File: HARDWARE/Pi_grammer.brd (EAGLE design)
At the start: 85.1 x 78.7 mm, 28 parts, among them J2 TARGET_copy, J3 TESTBED, J4 CABLE, U1 AT42QT1010SOT23

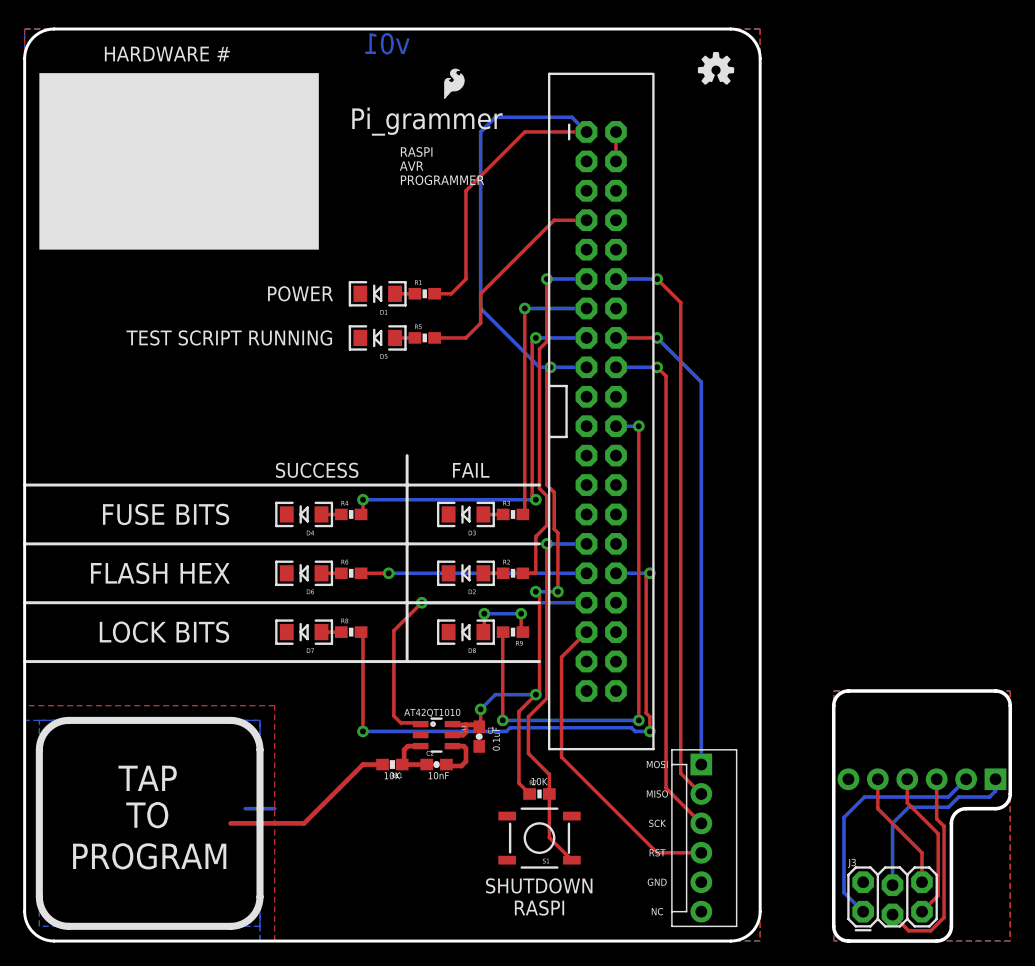
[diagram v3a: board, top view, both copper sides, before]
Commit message: changes "script running" led silk to "STAT"
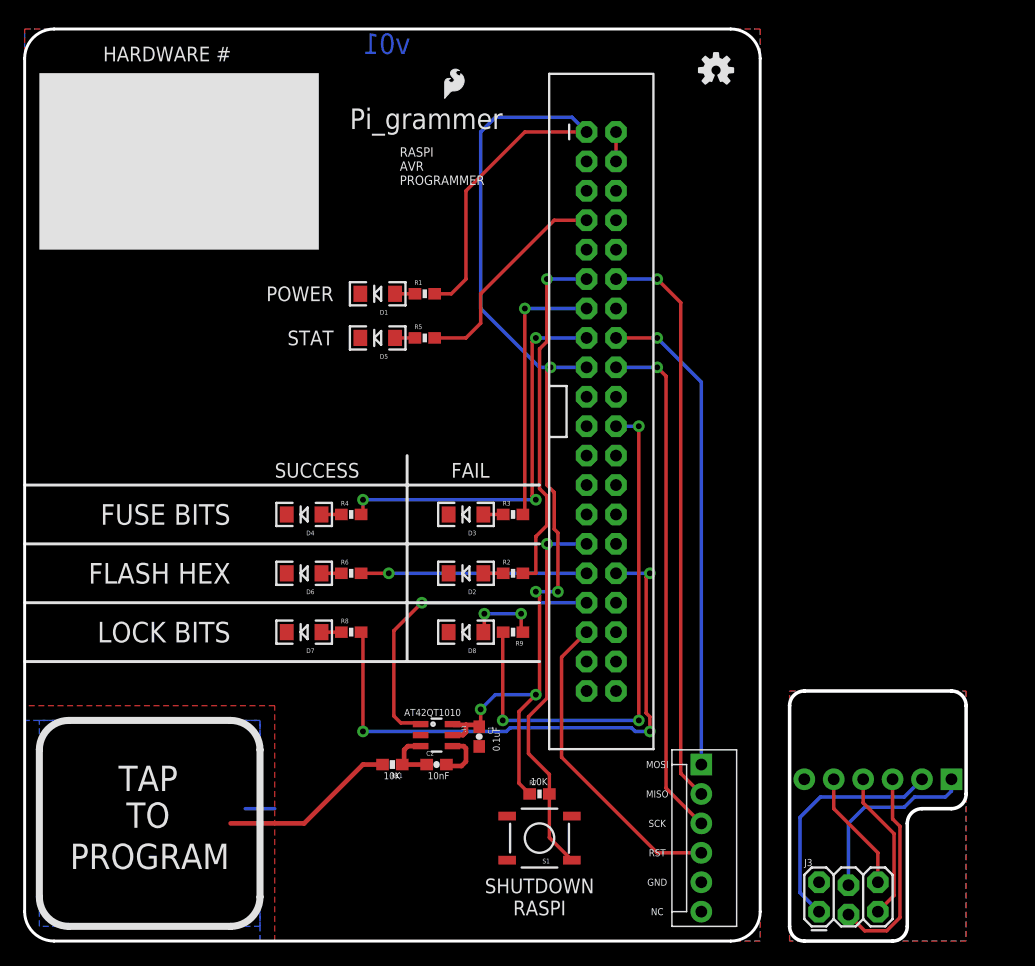
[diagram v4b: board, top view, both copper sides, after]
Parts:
- moved J3 3.81 mm to (68.6, 2.54)
- moved J4 3.81 mm to (80.0, 14.0)
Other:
- board size 85.1 x 78.7 mm -> 81.3 x 78.7 mm
- board text added: "STAT"
- board text removed: "TEST SCRIPT RUNNING"
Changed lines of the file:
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@@
 <layer number="47" name="Measures" color="7" fill="1" visible="no" active="yes"/>
 <layer number="48" name="Document" color="7" fill="1" visible="no" active="yes"/>
-<layer number="49" name="Reference" color="7" fill="1" visible="yes" active="yes"/>
+<layer number="49" name="Reference" color="7" fill="1" visible="no" active="yes"/>
 <layer number="50" name="dxf" color="7" fill="1" visible="no" active="yes"/>
 <layer number="51" name="tDocu" color="6" fill="1" visible="yes" active="yes"/>
@@
 <text x="28.067" y="70.104" size="1.778" layer="21" font="vector" ratio="15">Pi_grammer</text>
 <text x="6.7724375" y="75.946675" size="1.27" layer="21" font="vector" ratio="15">HARDWARE #</text>
-<text x="26.67" y="52.07" size="1.27" layer="21" font="vector" ratio="15" align="center-right">TEST SCRIPT RUNNING</text>
+<text x="26.67" y="52.07" size="1.27" layer="21" font="vector" ratio="15" align="center-right">STAT</text>
 <text x="17.78" y="36.83" size="1.778" layer="21" font="vector" ratio="15" align="center-right">FUSE BITS</text>
 <text x="26.67" y="55.88" size="1.27" layer="21" font="vector" ratio="15" align="center-right">POWER</text>
@@
 <text x="54.61" y="5.08" size="0.6096" layer="21" font="vector" ratio="15" align="center">GND</text>
 <text x="54.61" y="2.54" size="0.6096" layer="21" font="vector" ratio="15" align="center">NC</text>
-<wire x1="80.01" y1="1.27" x2="78.74" y2="0" width="0.3048" layer="20" curve="-90"/>
-<wire x1="78.74" y1="0" x2="71.12" y2="0" width="0.3048" layer="20"/>
-<wire x1="71.12" y1="0" x2="69.85" y2="1.27" width="0.3048" layer="20" curve="-90"/>
-<wire x1="69.85" y1="1.27" x2="69.85" y2="20.32" width="0.3048" layer="20"/>
-<wire x1="69.85" y1="20.32" x2="71.12" y2="21.59" width="0.3048" layer="20" curve="-90"/>
-<wire x1="71.12" y1="21.59" x2="83.82" y2="21.59" width="0.3048" layer="20"/>
-<wire x1="83.82" y1="21.59" x2="85.09" y2="20.32" width="0.3048" layer="20" curve="-90"/>
-<wire x1="85.09" y1="20.32" x2="85.09" y2="12.7" width="0.3048" layer="20"/>
-<wire x1="85.09" y1="12.7" x2="83.82" y2="11.43" width="0.3048" layer="20" curve="-90"/>
-<wire x1="83.82" y1="11.43" x2="81.28" y2="11.43" width="0.3048" layer="20"/>
-<wire x1="81.28" y1="11.43" x2="80.01" y2="10.16" width="0.3048" layer="20" curve="90"/>
-<wire x1="80.01" y1="10.16" x2="80.01" y2="1.27" width="0.3048" layer="20"/>
+<wire x1="76.2" y1="1.27" x2="74.93" y2="0" width="0.3048" layer="20" curve="-90"/>
+<wire x1="74.93" y1="0" x2="67.31" y2="0" width="0.3048" layer="20"/>
+<wire x1="67.31" y1="0" x2="66.04" y2="1.27" width="0.3048" layer="20" curve="-90"/>
+<wire x1="66.04" y1="1.27" x2="66.04" y2="20.32" width="0.3048" layer="20"/>
+<wire x1="66.04" y1="20.32" x2="67.31" y2="21.59" width="0.3048" layer="20" curve="-90"/>
+<wire x1="67.31" y1="21.59" x2="80.01" y2="21.59" width="0.3048" layer="20"/>
+<wire x1="80.01" y1="21.59" x2="81.28" y2="20.32" width="0.3048" layer="20" curve="-90"/>
+<wire x1="81.28" y1="20.32" x2="81.28" y2="12.7" width="0.3048" layer="20"/>
+<wire x1="81.28" y1="12.7" x2="80.01" y2="11.43" width="0.3048" layer="20" curve="-90"/>
+<wire x1="80.01" y1="11.43" x2="77.47" y2="11.43" width="0.3048" layer="20"/>
+<wire x1="77.47" y1="11.43" x2="76.2" y2="10.16" width="0.3048" layer="20" curve="90"/>
+<wire x1="76.2" y1="10.16" x2="76.2" y2="1.27" width="0.3048" layer="20"/>
 </plain>
 <attributes>
@@
 </element>
 <element name="J2" library="SparkFun-Connectors" package="MOLEX-1X6" value="TARGET_copy" x="58.42" y="15.24" rot="R270"/>
-<element name="J3" library="SparkFun-Connectors" package="2X3_LOCK" value="TESTBED" x="72.39" y="2.54"/>
-<element name="J4" library="SparkFun-Connectors" package="MOLEX-1X6-RA" value="CABLE" x="83.82" y="13.97" rot="MR0"/>
+<element name="J3" library="SparkFun-Connectors" package="2X3_LOCK" value="TESTBED" x="68.58" y="2.54"/>
+<element name="J4" library="SparkFun-Connectors" package="MOLEX-1X6-RA" value="CABLE" x="80.01" y="13.97" rot="MR0"/>
 </elements>
 <signals>
@@
 <contactref element="J4" pad="1"/>
 <contactref element="J3" pad="4"/>
-<wire x1="83.82" y1="13.97" x2="83.82" y2="12.954" width="0.3048" layer="16"/>
-<wire x1="83.82" y1="12.954" x2="83.312" y2="12.446" width="0.3048" layer="16"/>
-<wire x1="83.312" y1="12.446" x2="80.645" y2="12.446" width="0.3048" layer="16"/>
-<wire x1="80.645" y1="12.446" x2="79.756" y2="11.557" width="0.3048" layer="16"/>
-<wire x1="79.756" y1="11.557" x2="76.327" y2="11.557" width="0.3048" layer="16"/>
-<wire x1="76.327" y1="11.557" x2="74.93" y2="10.16" width="0.3048" layer="16"/>
-<wire x1="74.93" y1="10.16" x2="74.93" y2="4.826" width="0.3048" layer="16"/>
+<wire x1="80.01" y1="13.97" x2="80.01" y2="12.954" width="0.3048" layer="16"/>
+<wire x1="80.01" y1="12.954" x2="79.502" y2="12.446" width="0.3048" layer="16"/>
+<wire x1="79.502" y1="12.446" x2="76.835" y2="12.446" width="0.3048" layer="16"/>
+<wire x1="76.835" y1="12.446" x2="75.946" y2="11.557" width="0.3048" layer="16"/>
+<wire x1="75.946" y1="11.557" x2="72.517" y2="11.557" width="0.3048" layer="16"/>
+<wire x1="72.517" y1="11.557" x2="71.12" y2="10.16" width="0.3048" layer="16"/>
+<wire x1="71.12" y1="10.16" x2="71.12" y2="4.826" width="0.3048" layer="16"/>
 </signal>
 <signal name="MISO_C">
 <contactref element="J4" pad="2"/>
 <contactref element="J3" pad="1"/>
-<wire x1="81.28" y1="13.97" x2="79.756" y2="12.446" width="0.3048" layer="16"/>
-<wire x1="79.756" y1="12.446" x2="72.517" y2="12.446" width="0.3048" layer="16"/>
-<wire x1="72.517" y1="12.446" x2="70.739" y2="10.668" width="0.3048" layer="16"/>
-<wire x1="70.739" y1="10.668" x2="70.739" y2="4.191" width="0.3048" layer="16"/>
-<wire x1="70.739" y1="4.191" x2="72.39" y2="2.54" width="0.3048" layer="16"/>
+<wire x1="77.47" y1="13.97" x2="75.946" y2="12.446" width="0.3048" layer="16"/>
+<wire x1="75.946" y1="12.446" x2="68.707" y2="12.446" width="0.3048" layer="16"/>
+<wire x1="68.707" y1="12.446" x2="66.929" y2="10.668" width="0.3048" layer="16"/>
+<wire x1="66.929" y1="10.668" x2="66.929" y2="4.191" width="0.3048" layer="16"/>
+<wire x1="66.929" y1="4.191" x2="68.58" y2="2.54" width="0.3048" layer="16"/>
 </signal>
 <signal name="SCK_C">
 <contactref element="J3" pad="3"/>
 <contactref element="J4" pad="3"/>
-<wire x1="78.74" y1="13.97" x2="78.74" y2="10.541" width="0.3048" layer="1"/>
-<wire x1="78.74" y1="10.541" x2="79.375" y2="9.906" width="0.3048" layer="1"/>
-<wire x1="79.375" y1="9.906" x2="79.375" y2="2.032" width="0.3048" layer="1"/>
-<wire x1="79.375" y1="2.032" x2="78.232" y2="0.889" width="0.3048" layer="1"/>
-<wire x1="78.232" y1="0.889" x2="76.327" y2="0.889" width="0.3048" layer="1"/>
-<wire x1="76.327" y1="0.889" x2="74.93" y2="2.286" width="0.3048" layer="1"/>
+<wire x1="74.93" y1="13.97" x2="74.93" y2="10.541" width="0.3048" layer="1"/>
+<wire x1="74.93" y1="10.541" x2="75.565" y2="9.906" width="0.3048" layer="1"/>
+<wire x1="75.565" y1="9.906" x2="75.565" y2="2.032" width="0.3048" layer="1"/>
+<wire x1="75.565" y1="2.032" x2="74.422" y2="0.889" width="0.3048" layer="1"/>
+<wire x1="74.422" y1="0.889" x2="72.517" y2="0.889" width="0.3048" layer="1"/>
+<wire x1="72.517" y1="0.889" x2="71.12" y2="2.286" width="0.3048" layer="1"/>
 </signal>
 <signal name="RST_C">
 <contactref element="J4" pad="4"/>
 <contactref element="J3" pad="5"/>
-<wire x1="76.2" y1="13.97" x2="76.2" y2="11.938" width="0.3048" layer="1"/>
-<wire x1="78.867" y1="9.271" x2="78.867" y2="3.937" width="0.3048" layer="1"/>
-<wire x1="78.867" y1="3.937" x2="77.47" y2="2.54" width="0.3048" layer="1"/>
-<wire x1="76.2" y1="11.938" x2="78.867" y2="9.271" width="0.3048" layer="1"/>
+<wire x1="72.39" y1="13.97" x2="72.39" y2="11.938" width="0.3048" layer="1"/>
+<wire x1="75.057" y1="9.271" x2="75.057" y2="3.937" width="0.3048" layer="1"/>
+<wire x1="75.057" y1="3.937" x2="73.66" y2="2.54" width="0.3048" layer="1"/>
+<wire x1="72.39" y1="11.938" x2="75.057" y2="9.271" width="0.3048" layer="1"/>
 </signal>
 <signal name="GND_C">
 <contactref element="J4" pad="5"/>
 <contactref element="J3" pad="6"/>
-<wire x1="73.66" y1="13.97" x2="73.66" y2="11.43" width="0.3048" layer="1"/>
+<wire x1="69.85" y1="13.97" x2="69.85" y2="11.43" width="0.3048" layer="1"/>
 <polygon width="0.3048" layer="16" isolate="0.3048">
-<vertex x="85.09" y="0"/>
-<vertex x="69.85" y="0"/>
-<vertex x="69.85" y="21.59"/>
-<vertex x="85.09" y="21.59"/>
+<vertex x="81.28" y="0"/>
+<vertex x="66.04" y="0"/>
+<vertex x="66.04" y="21.59"/>
+<vertex x="81.28" y="21.59"/>
 </polygon>
 <polygon width="0.3048" layer="1" isolate="0.3048">
-<vertex x="85.09" y="0"/>
-<vertex x="69.85" y="0"/>
-<vertex x="69.85" y="21.59"/>
-<vertex x="85.09" y="21.59"/>
+<vertex x="81.28" y="0"/>
+<vertex x="66.04" y="0"/>
+<vertex x="66.04" y="21.59"/>
+<vertex x="81.28" y="21.59"/>
 </polygon>
-<wire x1="73.66" y1="11.43" x2="77.47" y2="7.62" width="0.3048" layer="1"/>
-<wire x1="77.47" y1="7.62" x2="77.47" y2="5.08" width="0.3048" layer="1"/>
+<wire x1="69.85" y1="11.43" x2="73.66" y2="7.62" width="0.3048" layer="1"/>
+<wire x1="73.66" y1="7.62" x2="73.66" y2="5.08" width="0.3048" layer="1"/>
 </signal>
 </signals>

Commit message: PROD_IDs to all populated parts, SCH cleanup
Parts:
- added FRAME1: FRAME-LETTER, SparkFun-Aesthetics:CREATIVE_COMMONS
- R1, R2, R3, R4, R5, R6, R7, R8, R9: device SparkFun-Resistors:0603-RES@1 -> SparkFun-Resistors:0603-RES
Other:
- board text added: "Pete Lewis"

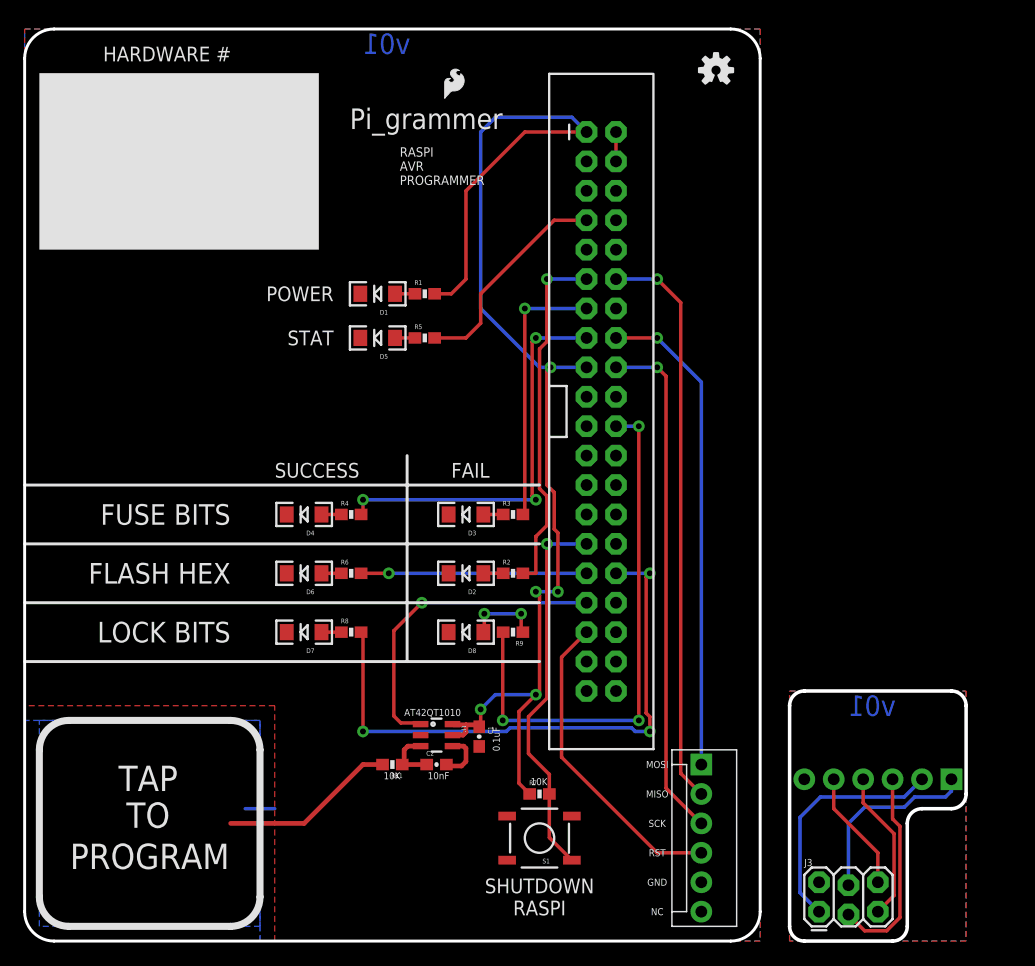
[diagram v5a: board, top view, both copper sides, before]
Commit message: added fiducials
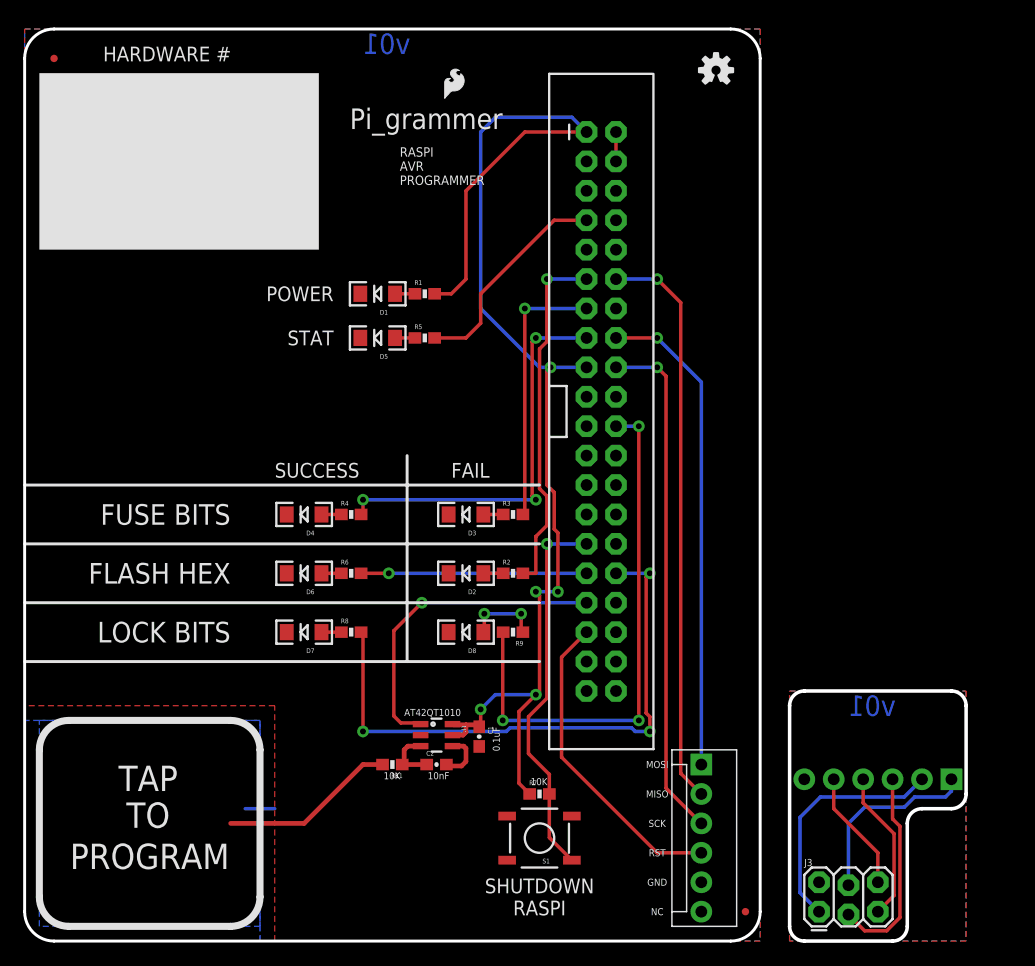
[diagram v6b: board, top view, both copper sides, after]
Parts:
- added FD1, FD2: FIDUCIALUFIDUCIAL, SparkFun-Aesthetics:FIDUCIAL-MICRO
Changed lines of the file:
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@@
 <?xml version="1.0" encoding="utf-8"?>
 <!DOCTYPE eagle SYSTEM "eagle.dtd">
-<eagle version="6.5.0">
+<eagle version="7.6.0">
 <drawing>
 <settings>
@@
 <pass name="Default">
 <param name="RoutingGrid" value="50mil"/>
+<param name="AutoGrid" value="1"/>
+<param name="Efforts" value="0"/>
+<param name="TopRouterVariant" value="1"/>
 <param name="tpViaShape" value="round"/>
 <param name="PrefDir.1" value="|"/>
@@
 </element>
 <element name="FRAME1" library="SparkFun-Aesthetics" package="CREATIVE_COMMONS" value="FRAME-LETTER" x="21.59" y="-21.59"/>
+<element name="FD1" library="SparkFun-Aesthetics" package="FIDUCIAL-MICRO" value="FIDUCIALUFIDUCIAL" x="2.54" y="76.2"/>
+<element name="FD2" library="SparkFun-Aesthetics" package="FIDUCIAL-MICRO" value="FIDUCIALUFIDUCIAL" x="62.23" y="2.54"/>
 </elements>
 <signals>

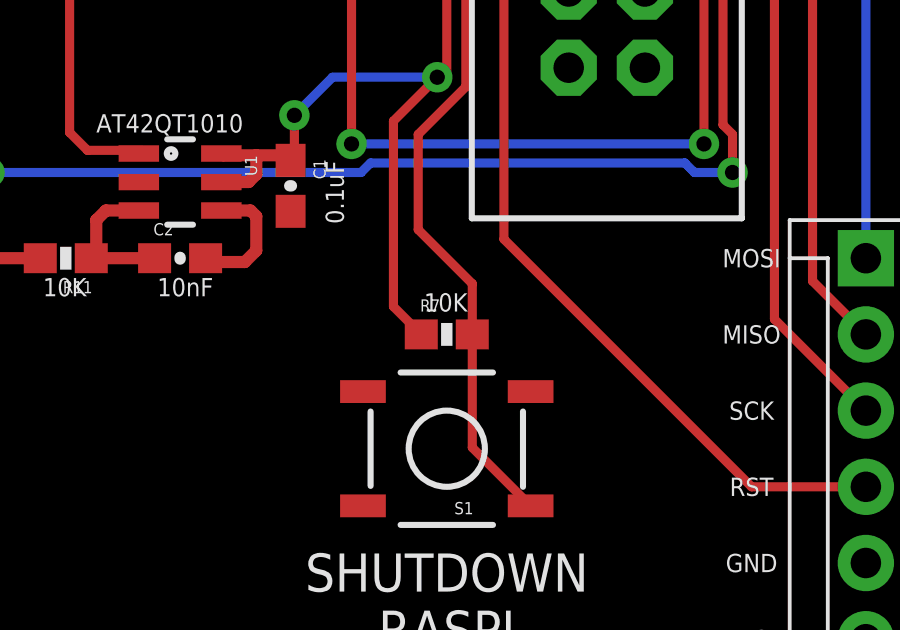
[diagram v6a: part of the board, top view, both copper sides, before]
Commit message: Changed value of R7 to 1K
This is the pullup resistor on the SHUTDOWN line/button. I was seeing
some strange behavior on a few shields that would actually cause a
shutdown right at bootup. Getting a little more current on this pullup
seems to have solved the issue.
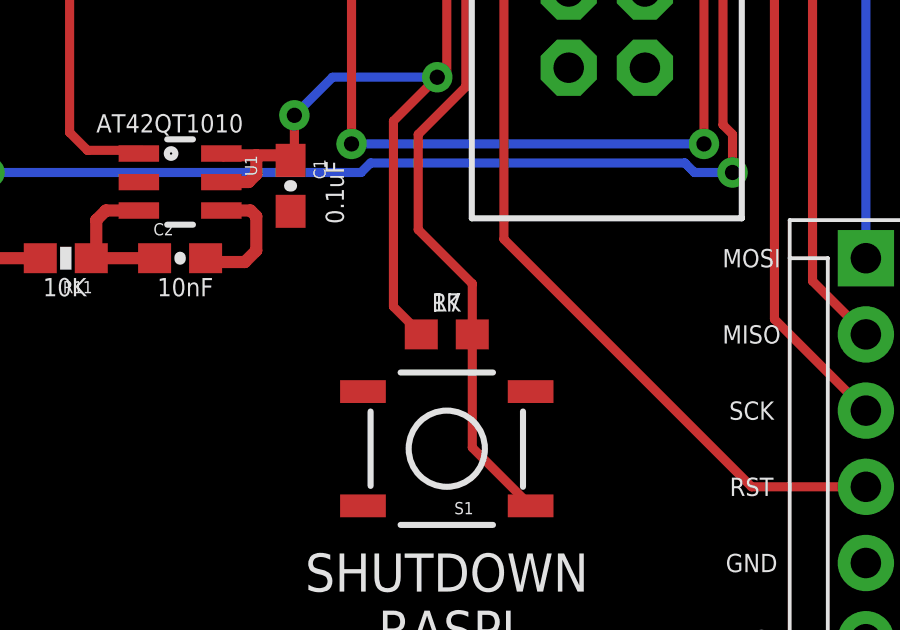
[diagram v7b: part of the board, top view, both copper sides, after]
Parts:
- R7: value 10K -> 1k; device SparkFun-Resistors:0603-RES -> SparkFun-Resistors:0603
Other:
- board text added: "1K"
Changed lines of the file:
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@@
 <text x="17.78" y="26.67" size="1.778" layer="21" font="vector" ratio="15" align="center-right">LOCK BITS</text>
 <text x="29.21" y="77.47" size="1.778" layer="16" font="vector" ratio="21" rot="MR0" align="center-right">v01</text>
-<text x="43.688" y="13.462" size="0.6096" layer="21" font="vector" ratio="15">10K</text>
+<text x="43.942" y="13.462" size="0.6096" layer="21" font="vector" ratio="15">1K</text>
 <text x="21.59" y="40.64" size="1.27" layer="21" font="vector" ratio="15" rot="R180" align="center-right">SUCCESS</text>
 <wire x1="20.32" y1="16.51" x2="17.78" y2="19.05" width="0.6096" layer="21" curve="90"/>
@@
 <attribute name="PROD_ID" value="SWCH-08247" x="44.45" y="8.89" size="1.778" layer="27" font="vector" ratio="15" rot="R180" display="off"/>
 </element>
-<element name="R7" library="SparkFun-Resistors" package="0603-RES" value="10K" x="44.45" y="12.7">
-<attribute name="PROD_ID" value="RES-00824" x="44.45" y="12.7" size="1.778" layer="27" font="vector" ratio="15" display="off"/>
+<element name="R7" library="SparkFun-Resistors" package="0603" value="1k" x="44.45" y="12.7">
+<attribute name="PROD_ID" value="RES-07856" x="44.45" y="12.7" size="1.778" layer="27" font="vector" ratio="15" display="off"/>
 </element>
 <element name="R8" library="SparkFun-Resistors" package="0603-RES" value="1K" x="28.194" y="26.67">
